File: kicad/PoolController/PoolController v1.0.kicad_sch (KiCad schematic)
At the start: 61 parts, among them J1 Pompe Péristaltique, J2 Pompe Péristaltique, J4 Sonde température DS18B20, J5 Contacteur Puissance Filtrati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, J6 Conn_01x03, J7 Conn_01x03, J8 Contacteur Puissance Eclairage, J9 Alimentation 12V (2A min), Q2 IRLZ44N, Q4 IRLZ44N, Q5 IRF4905, Q6 IRLZ44N, Q7 IRLZ44N, U1 LM7805_TO220, U2 ESP32-DevKitC, U3 D24V10F3

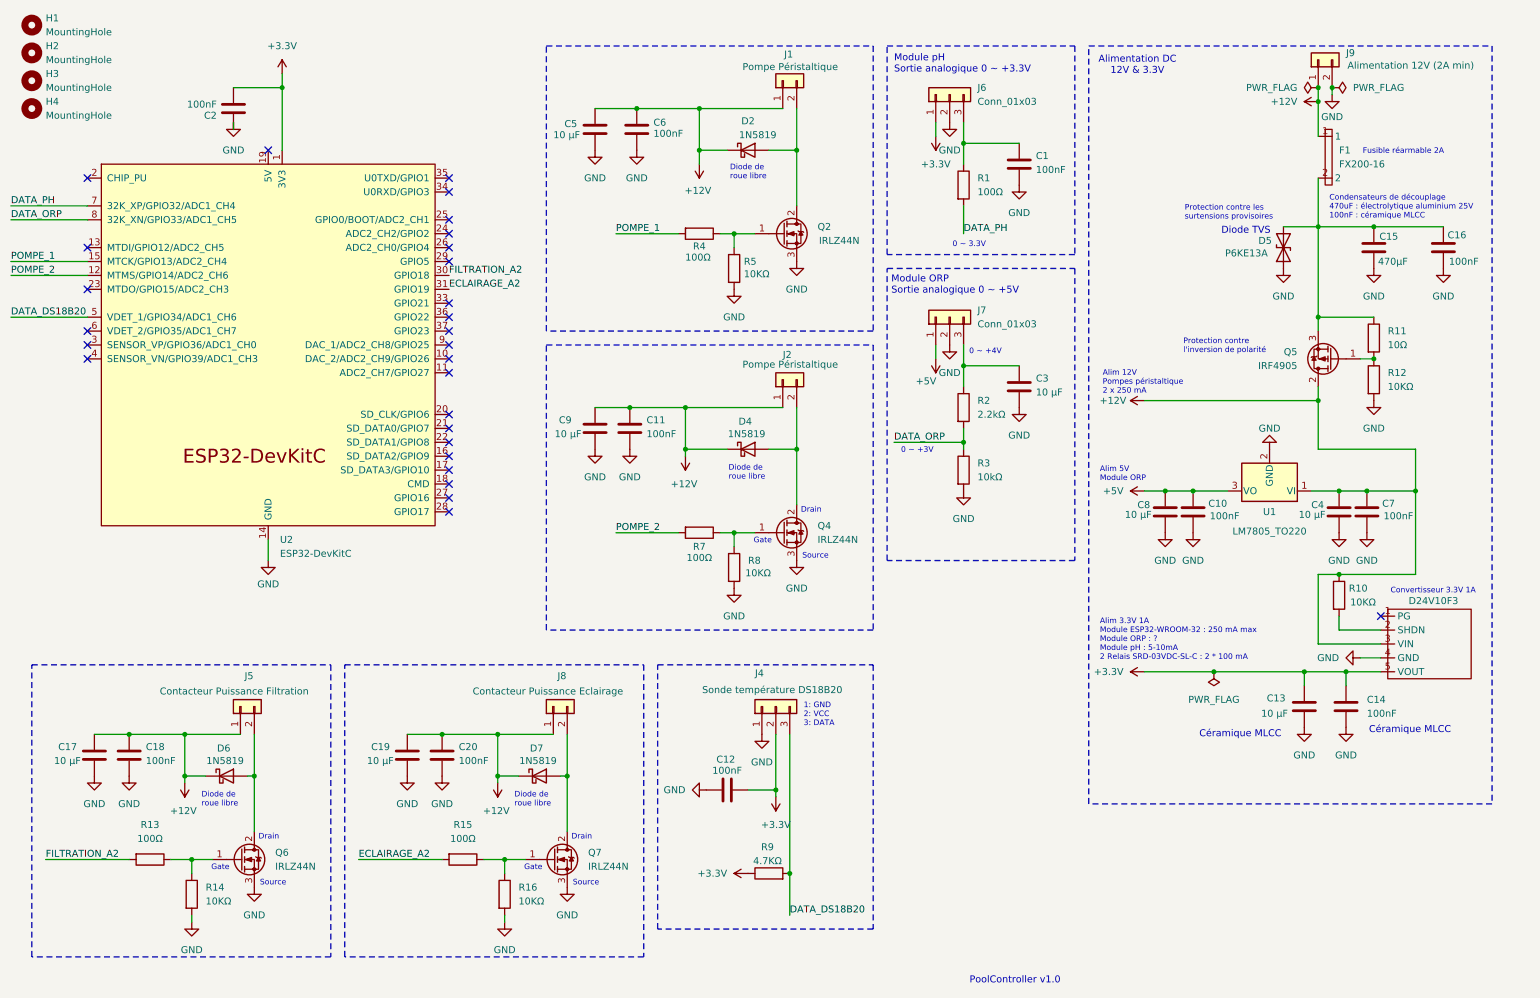
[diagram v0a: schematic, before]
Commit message: Préparation pour publication GitHub
Mise à jour complète de la documentation et nettoyage pour publication:

Documentation:
- Mise à jour README avec dernières fonctionnalités (PWM 20kHz, test pompes, ADS1115)
- Ajout schéma de câblage détaillé avec MOSFETs IRLZ44N
- Documentation calibration pH DFRobot et ORP via interface web
- Ajout changelog version 2025.12.6
- Ajout LICENSE MIT

Configuration:
- .gitignore: Exclusion des fichiers binaires (*.bin, *.elf)
- .gitignore: Exclusion des backups KiCad automatiques
- Nettoyage fichiers KiCad (suppression auto-save et anciens backups)

Corrections:
- src/mqtt_manager.cpp: Corrections mineures

🤖 Generated with [Claude Code](https://claude.com/claude-code)

Co-Authored-By: Claude Sonnet 4.5 <noreply@anthropic.com>
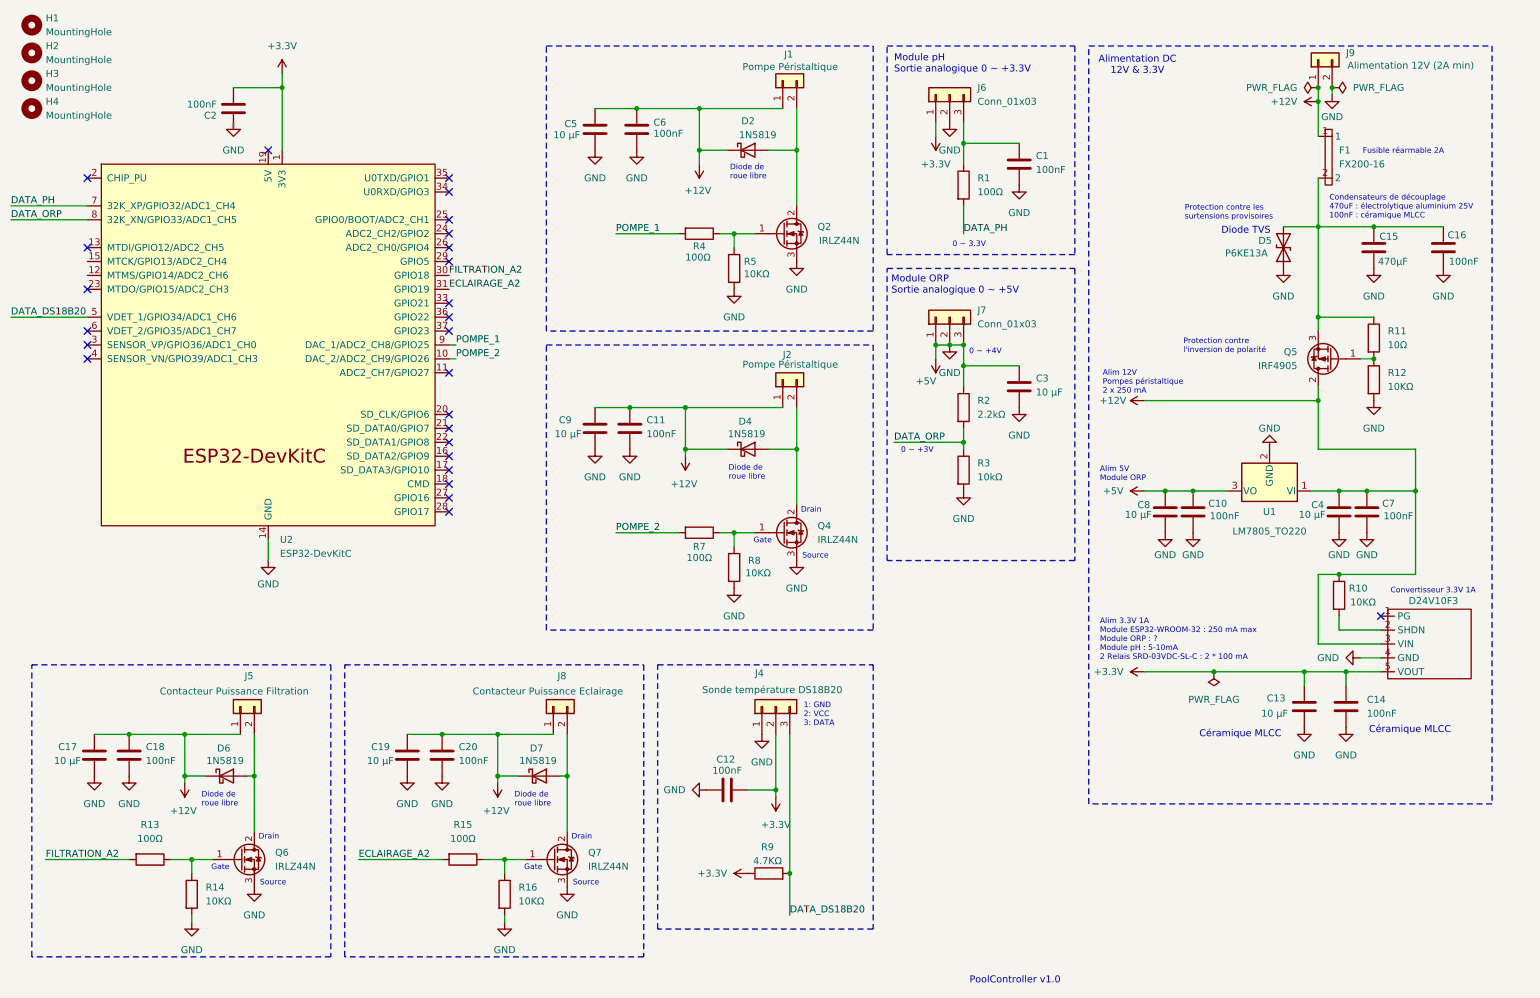
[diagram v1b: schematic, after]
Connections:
- net GND is gone; now on net +5V: C1.2, C10.2, C11.2, C12.1, C13.2, C14.2, C15.2, C16.2, C17.2, C18.2, C19.2, C2.1, C20.2, C3.2, C4.2, C5.2, C6.2, C7.2, C8.2, C9.2, D5.1 (A1), J4.1 (Pin_1), J6.2 (Pin_2), J7.2 (Pin_2), J9.2 (Pin_2), Q2.3 (S), Q4.3 (S), Q6.3 (S), Q7.3 (S), R12.2, R14.2, R16.2, R3.2, R5.2, R8.2, U1.2 (GND), U2.14 (GND), U2.32 (GND), U2.38 (GND), U3.4 (GND)
- net +5V: now also C3.1, J7.3 (Pin_3), R2.1
- net POMPE_1: now also U2.9 (DAC_1/ADC2_CH8/GPIO25); no longer U2.15 (MTCK/GPIO13/ADC2_CH4)
- net POMPE_2: now also U2.10 (DAC_2/ADC2_CH9/GPIO26); no longer U2.12 (MTMS/GPIO14/ADC2_CH6)
- no-connect marks 28 -> 26
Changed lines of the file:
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@@
 	)
 	(junction
+		(at 184.15 73.66)
+		(diameter 0)
+		(color 0 0 0 0)
+	)
+	(junction
 		(at 91.44 144.78)
 		(diameter 0)
@@
 	)
 	(junction
+		(at 181.61 73.66)
+		(diameter 0)
+		(color 0 0 0 0)
+	)
+	(junction
 		(at 114.3 152.4)
 		(diameter 0)
@@
 	)
 	(junction
+		(at 186.69 73.66)
+		(diameter 0)
+		(color 0 0 0 0)
+	)
+	(junction
 		(at 57.15 152.4)
 		(diameter 0)
@@
 	)
 	(no_connect
-		(at 92.71 76.2)
-	)
-	(no_connect
 		(at 59.69 38.1)
 	)
@@
 	)
 	(no_connect
-		(at 92.71 73.66)
-	)
-	(no_connect
 		(at 92.71 93.98)
 	)
@@
 	(wire
 		(pts
+			(xy 184.15 73.66) (xy 186.69 73.66)
+		)
+		(stroke
+			(width 0)
+			(type default)
+		)
+	)
+	(wire
+		(pts
 			(xy 251.46 128.27) (xy 262.89 128.27)
 		)
@@
 	(wire
 		(pts
+			(xy 181.61 73.66) (xy 184.15 73.66)
+		)
+		(stroke
+			(width 0)
+			(type default)
+		)
+	)
+	(wire
+		(pts
 			(xy 156.21 92.71) (xy 156.21 102.87)
 		)
@@
 	(wire
 		(pts
-			(xy 12.7 60.96) (xy 26.67 60.96)
-		)
-		(stroke
-			(width 0)
-			(type default)
-		)
-	)
-	(wire
-		(pts
 			(xy 256.54 133.35) (xy 256.54 135.89)
 		)
@@
 	(wire
 		(pts
-			(xy 251.46 68.58) (xy 251.46 71.12)
+			(xy 92.71 76.2) (xy 93.98 76.2)
 		)
 		(stroke
@@
 	(wire
 		(pts
-			(xy 269.24 100.33) (xy 269.24 115.57)
+			(xy 251.46 68.58) (xy 251.46 71.12)
 		)
 		(stroke
@@
 	(wire
 		(pts
-			(xy 245.11 52.07) (xy 251.46 52.07)
+			(xy 269.24 100.33) (xy 269.24 115.57)
 		)
 		(stroke
@@
 	(wire
 		(pts
-			(xy 251.46 29.21) (xy 251.46 35.56)
+			(xy 245.11 52.07) (xy 251.46 52.07)
 		)
 		(stroke
@@
 	(wire
 		(pts
-			(xy 76.2 167.64) (xy 91.44 167.64)
+			(xy 251.46 29.21) (xy 251.46 35.56)
 		)
 		(stroke
@@
 	(wire
 		(pts
-			(xy 12.7 58.42) (xy 26.67 58.42)
+			(xy 76.2 167.64) (xy 91.44 167.64)
 		)
 		(stroke
@@
 	(wire
 		(pts
+			(xy 92.71 73.66) (xy 93.98 73.66)
+		)
+		(stroke
+			(width 0)
+			(type default)
+		)
+	)
+	(wire
+		(pts
 			(xy 186.69 77.47) (xy 186.69 81.28)
 		)
@@
 	)
 	(label "POMPE_2"
-		(at 12.7 60.96 0)
+		(at 93.98 76.2 0)
 		(effects
 			(font
@@
 	)
 	(label "POMPE_1"
-		(at 12.7 58.42 0)
+		(at 93.98 73.66 0)
 		(effects
 			(font
@@
 		(on_board yes)
 		(dnp no)
-		(fields_autoplaced yes)
 		(property "Reference" "#PWR014"
 			(at 260.35 114.3 0)
@@
 		)
 		(property "Value" "GND"
-			(at 260.35 113.03 0)
+			(at 260.35 112.014 0)
 			(effects
 				(font
@@
 		(on_board yes)
 		(dnp no)
-		(fields_autoplaced yes)
 		(property "Reference" "#PWR017"
 			(at 228.6 114.3 0)
@@
 		)
 		(property "Value" "GND"
-			(at 228.6 113.03 0)
+			(at 228.6 112.014 0)
 			(effects
 				(font
@@
 		(on_board yes)
 		(dnp no)
-		(fields_autoplaced yes)
 		(property "Reference" "#PWR012"
 			(at 255.27 114.3 0)
@@
 		)
 		(property "Value" "GND"
-			(at 255.27 113.03 0)
+			(at 255.27 112.014 0)
 			(effects
 				(font
@@
 		(on_board yes)
 		(dnp no)
-		(fields_autoplaced yes)
 		(property "Reference" "#PWR015"
 			(at 223.52 114.3 0)
@@
 		)
 		(property "Value" "GND"
-			(at 223.52 113.03 0)
+			(at 223.52 112.014 0)
 			(effects
 				(font
